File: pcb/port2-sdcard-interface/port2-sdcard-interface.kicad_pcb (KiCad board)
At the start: 4 copper layers, 80 x 100 mm, 58 parts, among them J2 P2000T Port 2, J3 SD Card, U1 CY62128ELL-45SXI, U10 74HC32, U11 74HC273, U12 74HC165, U13 74HC595, U14 74HC00, U15 SST39SF010, U17 74HC138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

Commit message: Adding secondary LEDs
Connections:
- U4 pad 12: ~{S5} -> Net-(U4-Pad12)
- U4 pad 13: ~{S5} -> Net-(U4-Pad12)
- U9 pad 4: ~{S2} -> ~{S5}
- U9 pad 5: ~{RD} -> ~{WR}
- U9 pad 6: unconnected-(U9-Pad6) -> Net-(U4-Pad12)
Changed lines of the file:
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@@
   (net 81 "~{CLKSTART}")
   (net 82 "~{SER_RD}")
-  (net 83 "unconnected-(U9-Pad6)")
+  (net 83 "Net-(U4-Pad12)")
   (net 84 "~{SDOUT_SET}")
   (net 85 "~{SDOUT_RESET}")
@@
       (net 115 "LED_SEL") (pintype "output"))
     (pad "12" smd roundrect (at 2.475 1.27 270) (size 1.95 0.6) (layers "B.Cu" "B.Paste" "B.Mask") (roundrect_rratio 0.25)
-      (net 116 "~{S5}") (pintype "input"))
+      (net 83 "Net-(U4-Pad12)") (pintype "input"))
     (pad "13" smd roundrect (at 2.475 2.54 270) (size 1.95 0.6) (layers "B.Cu" "B.Paste" "B.Mask") (roundrect_rratio 0.25)
-      (net 116 "~{S5}") (pintype "input"))
+      (net 83 "Net-(U4-Pad12)") (pintype "input"))
     (pad "14" smd roundrect (at 2.475 3.81 270) (size 1.95 0.6) (layers "B.Cu" "B.Paste" "B.Mask") (roundrect_rratio 0.25)
       (net 1 "VCC") (pinfunction "VCC") (pintype "power_in"))
@@
       (net 82 "~{SER_RD}") (pintype "output"))
     (pad "4" smd roundrect (at -2.475 0 270) (size 1.95 0.6) (layers "B.Cu" "B.Paste" "B.Mask") (roundrect_rratio 0.25)
-      (net 79 "~{S2}") (pintype "input"))
+      (net 116 "~{S5}") (pintype "input"))
     (pad "5" smd roundrect (at -2.475 -1.27 270) (size 1.95 0.6) (layers "B.Cu" "B.Paste" "B.Mask") (roundrect_rratio 0.25)
-      (net 31 "~{RD}") (pintype "input"))
+      (net 32 "~{WR}") (pintype "input"))
     (pad "6" smd roundrect (at -2.475 -2.54 270) (size 1.95 0.6) (layers "B.Cu" "B.Paste" "B.Mask") (roundrect_rratio 0.25)
-      (net 83 "unconnected-(U9-Pad6)") (pintype "output+no_connect"))
+      (net 83 "Net-(U4-Pad12)") (pintype "output"))
     (pad "7" smd roundrect (at -2.475 -3.81 270) (size 1.95 0.6) (layers "B.Cu" "B.Paste" "B.Mask") (roundrect_rratio 0.25)
       (net 12 "GND") (pinfunction "GND") (pintype "power_in"))
@@
     (connect_pads (clearance 0))
     (min_thickness 0.25) (filled_areas_thickness no)
-    (fill yes (thermal_gap 0.5) (thermal_bridge_width 0.5))
+    (fill (thermal_gap 0.5) (thermal_bridge_width 0.5))
     (polygon
       (pts
@@
     (connect_pads (clearance 0))
     (min_thickness 0.25) (filled_areas_thickness no)
-    (fill yes (thermal_gap 0.5) (thermal_bridge_width 0.5))
+    (fill (thermal_gap 0.5) (thermal_bridge_width 0.5))
     (polygon
       (pts

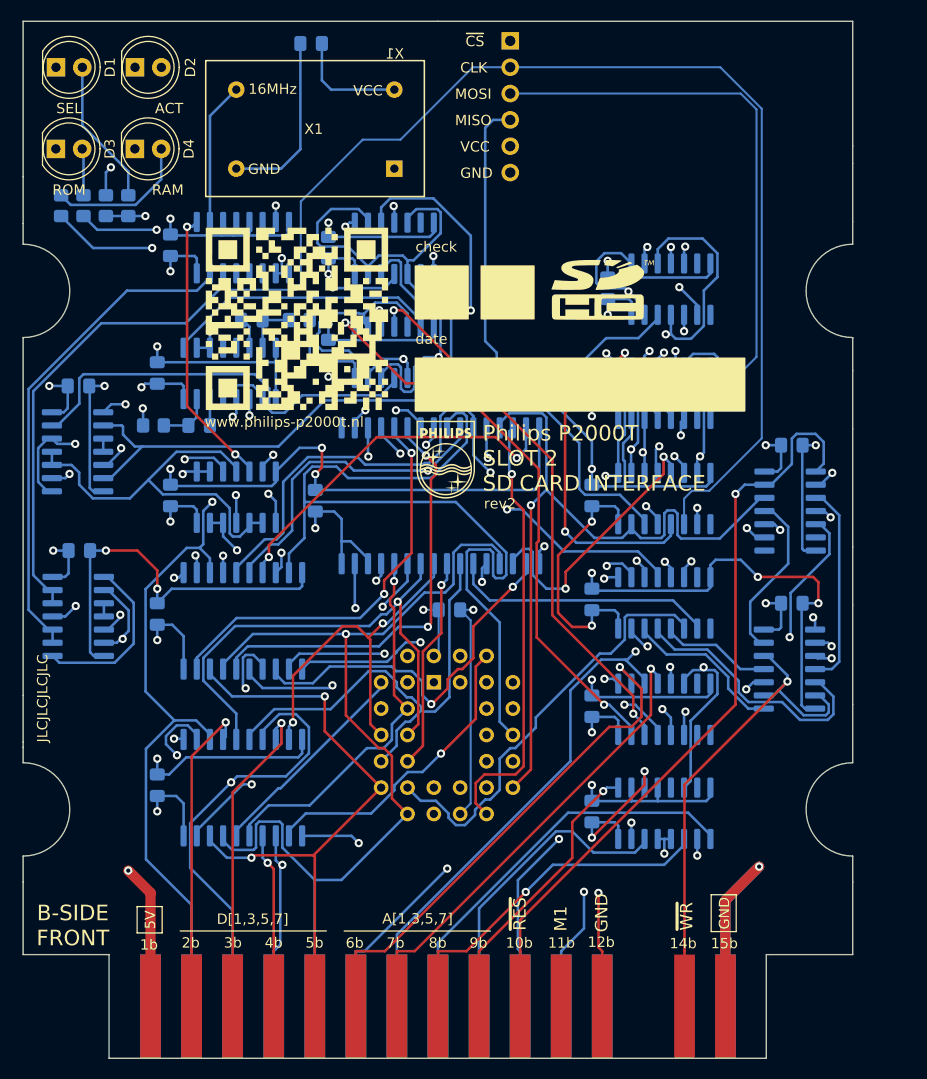
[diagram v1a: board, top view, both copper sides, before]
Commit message: Fixing bug in erroneously triggered LEDs
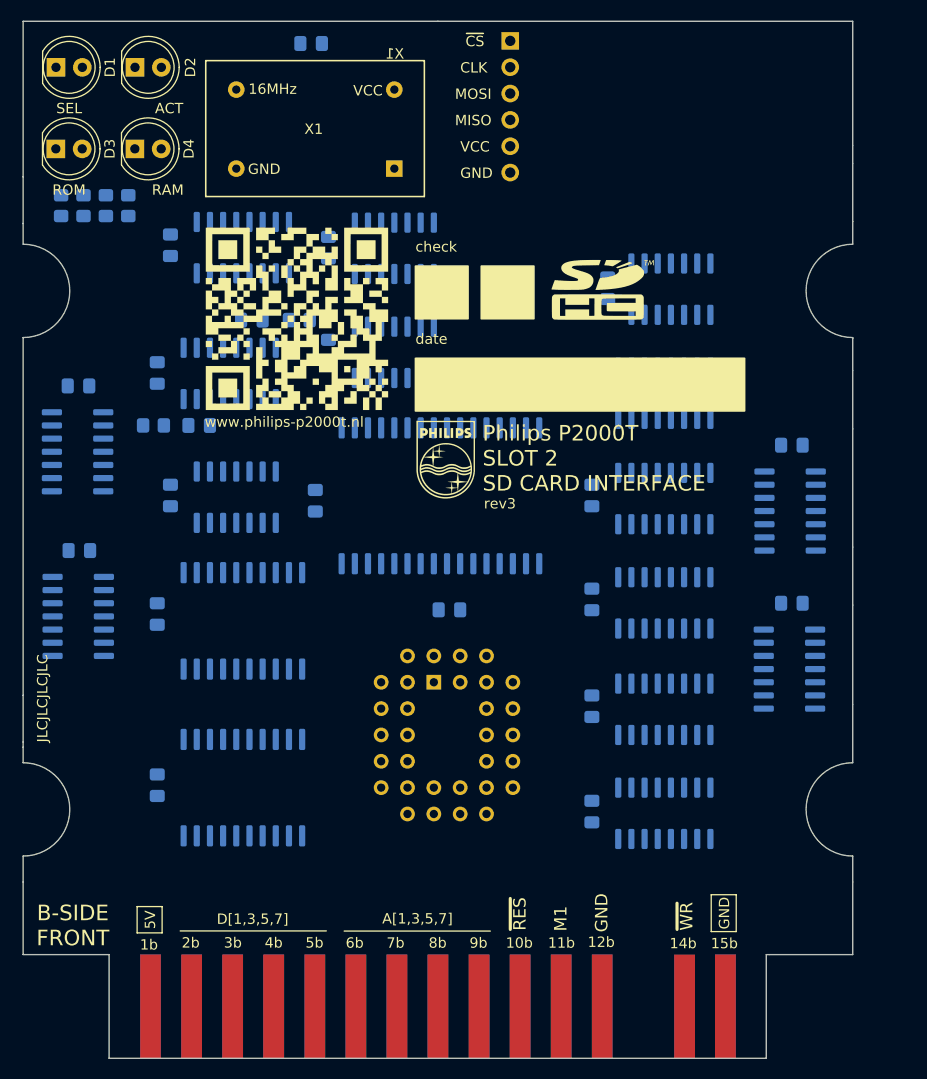
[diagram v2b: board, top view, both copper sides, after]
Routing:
- net GND: track 412.5 -> 0.00 mm, vias 26 -> 0
- net D0: track 230.2 -> 0.00 mm, vias 5 -> 0
- net VCC: track 197.2 -> 0.00 mm, vias 34 -> 0
- net ~{RES}: track 189.6 -> 0.00 mm, vias 4 -> 0
- net D1: track 158.9 -> 0.00 mm, vias 4 -> 0
- net ~{WR}: track 157.8 -> 0.00 mm, vias 4 -> 0
- net CLK: track 156.7 -> 0.00 mm
- net D2: track 152.9 -> 0.00 mm, vias 4 -> 0
- net D6: track 149.6 -> 0.00 mm, vias 3 -> 0
- net A3: track 143.2 -> 0.00 mm, vias 2 -> 0
- net D5: track 132.5 -> 0.00 mm, vias 5 -> 0
- net D7: track 127.4 -> 0.00 mm, vias 4 -> 0
- net D4: track 119.6 -> 0.00 mm, vias 5 -> 0
- net ~{RD}: track 118.8 -> 0.00 mm, vias 3 -> 0
- net D3: track 116.2 -> 0.00 mm, vias 4 -> 0
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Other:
- board text added: "rev3"
- board text removed: "rev2"

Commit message: Fixing bug in RAM/ROM leds
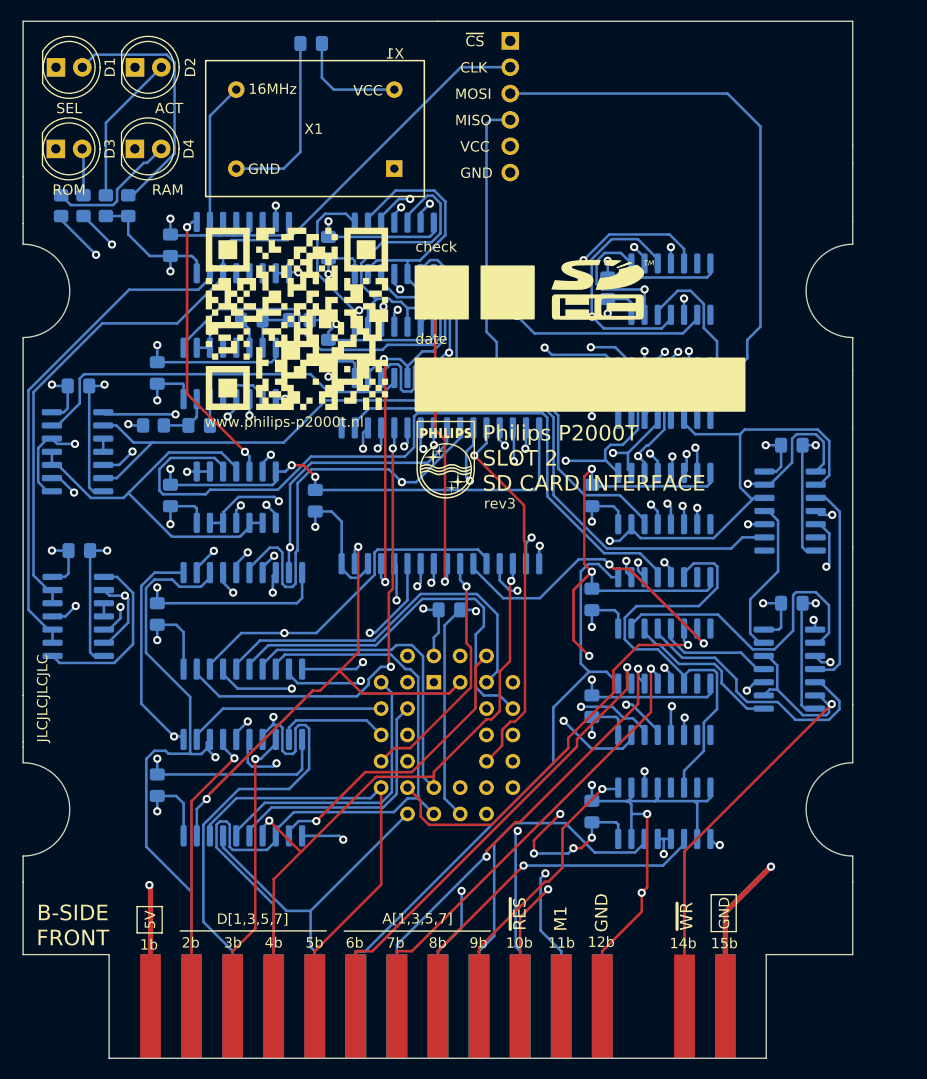
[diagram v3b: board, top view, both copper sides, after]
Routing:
- net GND: track 0.00 -> 419.8 mm, vias 0 -> 25
- net D0: track 0.00 -> 205.1 mm, vias 0 -> 4
- net VCC: track 0.00 -> 193.7 mm, vias 0 -> 37
- net ~{WR}: track 0.00 -> 176.8 mm, vias 0 -> 4
- net ~{RES}: track 0.00 -> 174.0 mm, vias 0 -> 4
- net D7: track 0.00 -> 156.4 mm, vias 0 -> 3
- net D1: track 0.00 -> 151.3 mm, vias 0 -> 4
- net D2: track 0.00 -> 138.7 mm, vias 0 -> 4
- net D4: track 0.00 -> 138.7 mm, vias 0 -> 3
- net A3: track 0.00 -> 134.3 mm, vias 0 -> 2
- net CLK: track 0.00 -> 133.2 mm, vias 0 -> 1
- net D5: track 0.00 -> 127.6 mm, vias 0 -> 4
- net D6: track 0.00 -> 125.8 mm, vias 0 -> 4
- net D3: track 0.00 -> 120.4 mm, vias 0 -> 4
- net ~{RD}: track 0.00 -> 107.2 mm, vias 0 -> 3
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
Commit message: Revising PCB
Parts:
- D3: value ROM -> READ
- D4: value RAM -> WRITE
- R1, R6, R7: value 510 -> 560
- R2: value 510 -> 0
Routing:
- net Net-(U3A-Q): track 62.7 -> 71.9 mm
- net Net-(U3B-Q): track 67.5 -> 73.1 mm
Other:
- board text added: "act"
- board text added: "https://github.com/ifilot/p2000t-sdcard"
- board text added: "read"
- board text added: "rev4"
- board text added: "sel"
- board text added: "write"
- board text removed: "rev3"
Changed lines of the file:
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@@
         (effects (font (size 1 1) (thickness 0.15)))
     )
-    (fp_text value "RAM" (at 3.175 3.96) (layer "F.SilkS")
+    (fp_text value "WRITE" (at 3.175 3.96) (layer "F.SilkS")
         (effects (font (size 1 1) (thickness 0.15)))
     )
@@
         (effects (font (size 1 1) (thickness 0.15)))
     )
-    (fp_text value "ROM" (at 1.27 3.96) (layer "F.SilkS")
+    (fp_text value "READ" (at 1.27 3.96) (layer "F.SilkS")
         (effects (font (size 1 1) (thickness 0.15)))
     )
@@
         (effects (font (size 1 1) (thickness 0.15)) (justify mirror))
     )
-    (fp_text value "510" (at 0 -1.65 90) (layer "B.Fab")
-        (effects (font (size 1 1) (thickness 0.15)) (justify mirror))
+    (fp_text value "560" (at -4.556 0.127 90) (layer "B.SilkS")
+        (effects (font (size 0.7 0.7) (thickness 0.1)) (justify mirror))
     )
     (fp_text user "${REFERENCE}" (at 0 0 90) (layer "B.Fab")
@@
         (effects (font (size 1 1) (thickness 0.15)) (justify mirror))
     )
-    (fp_text value "510" (at 0 -1.65 90) (layer "B.Fab")
-        (effects (font (size 1 1) (thickness 0.15)) (justify mirror))
+    (fp_text value "560" (at -4.556 0.381 270) (layer "B.SilkS")
+        (effects (font (size 0.7 0.7) (thickness 0.1) bold) (justify mirror))
     )
     (fp_text user "${REFERENCE}" (at 0 0 90) (layer "B.Fab")
@@
         (effects (font (size 1 1) (thickness 0.15)) (justify mirror))
     )
-    (fp_text value "510" (at 0 -1.65 90) (layer "B.Fab")
-        (effects (font (size 1 1) (thickness 0.15)) (justify mirror))
+    (fp_text value "560" (at 4.556 0.254 90) (layer "B.SilkS")
+        (effects (font (size 0.7 0.7) (thickness 0.1)) (justify mirror))
     )
     (fp_text user "${REFERENCE}" (at 0 0 90) (layer "B.Fab")
@@
         (effects (font (size 1 1) (thickness 0.15)) (justify mirror))
     )
-    (fp_text value "510" (at 0 -1.65 90) (layer "B.Fab")
-        (effects (font (size 1 1) (thickness 0.15)) (justify mirror))
+    (fp_text value "0" (at 3.794 0.254 90) (layer "B.SilkS")
+        (effects (font (size 0.7 0.7) (thickness 0.1)) (justify mirror))
     )
     (fp_text user "${REFERENCE}" (at 0 0 90) (layer "B.Fab")
@@
     (effects (font (size 1 1) (thickness 0.15)) (justify mirror))
   )
+  (gr_text "act" (at 29.953 31.736 90) (layer "B.SilkS")
+    (effects (font (size 0.7 0.7) (thickness 0.1)) (justify left bottom mirror))
+  )
   (gr_text "MISO" (at 64.751 27.926) (layer "B.SilkS")
     (effects (font (size 1 1) (thickness 0.15)) (justify left bottom mirror))
@@
     (effects (font (size 1 1) (thickness 0.15)) (justify left bottom mirror))
   )
+  (gr_text "sel" (at 32.112 31.99 90) (layer "B.SilkS")
+    (effects (font (size 0.7 0.7) (thickness 0.1)) (justify left bottom mirror))
+  )
+  (gr_text "read" (at 27.794 31.228 90) (layer "B.SilkS")
+    (effects (font (size 0.7 0.7) (thickness 0.1)) (justify left bottom mirror))
+  )
   (gr_text "2a" (at 37.7497 106.6421) (layer "B.SilkS")
     (effects (font (size 1 1) (thickness 0.15)) (justify mirror))
@@
     (effects (font (size 1.2 1.2) (thickness 0.3)) (justify mirror))
   )
+  (gr_text "write" (at 25.508 31.228 90) (layer "B.SilkS")
+    (effects (font (size 0.7 0.7) (thickness 0.1)) (justify left bottom mirror))
+  )
   (gr_text "MISO" (at 73.26 53.199) (layer "B.SilkS")
     (effects (font (size 1 1) (thickness 0.15)) (justify left bottom mirror))
@@
     (effects (font (size 1 1) (thickness 0.15)) (justify left bottom))
   )
-  (gr_text "rev3" (at 66.021 64.883) (layer "F.SilkS")
+  (gr_text "rev4" (at 66.021 64.883) (layer "F.SilkS")
     (effects (font (size 1 1) (thickness 0.15)) (justify left bottom))
   )
@@
     (effects (font (size 1 1) (thickness 0.15)))
   )
+  (gr_text "https://github.com/ifilot/p2000t-sdcard" (at 59.417 66.915) (layer "F.SilkS")
+    (effects (font (size 1 1) (thickness 0.15)) (justify left bottom))
+  )
   (gr_text "date" (at 59.417 49.008) (layer "F.SilkS")
     (effects (font (size 1 1) (thickness 0.15)) (justify left bottom))
@@
   (segment (start 94.3897 70.8312) (end 94.3897 65.9414) (width 0.25) (layer "B.Cu") (net 109))
   (segment (start 91.7087 73.5122) (end 94.3897 70.8312) (width 0.25) (layer "B.Cu") (net 109))
-  (via (at 30.16 39.3067) (size 0.8) (drill 0.4) (layers "F.Cu" "B.Cu") (net 113))
+  (via (at 29.445 44.436) (size 0.8) (drill 0.4) (layers "F.Cu" "B.Cu") (net 113))
   (via (at 75.6266 40.8266) (size 0.8) (drill 0.4) (layers "F.Cu" "B.Cu") (net 113))
-  (segment (start 75.6266 40.8266) (end 74.1067 39.3067) (width 0.25) (layer "In1.Cu") (net 113))
-  (segment (start 74.1067 39.3067) (end 30.16 39.3067) (width 0.25) (layer "In1.Cu") (net 113))
+  (segment (start 31.731 39.61) (end 29.445 41.896) (width 0.25) (layer "In1.Cu") (net 113))
+  (segment (start 75.6266 40.8266) (end 74.1525 39.3525) (width 0.25) (layer "In1.Cu") (net 113))
+  (segment (start 29.445 41.896) (end 29.445 44.436) (width 0.25) (layer "In1.Cu") (net 113))
+  (segment (start 74.1525 39.3525) (end 31.9885 39.3525) (width 0.25) (layer "In1.Cu") (net 113))
+  (segment (start 74.1525 39.3525) (end 74.1067 39.3067) (width 0.25) (layer "In1.Cu") (net 113))
+  (segment (start 31.9885 39.3525) (end 31.731 39.61) (width 0.25) (layer "In1.Cu") (net 113))
   (segment (start 85.325 41.137) (end 85.325 39.7371) (width 0.25) (layer "B.Cu") (net 113))
   (segment (start 78.1117 38.3415) (end 75.6266 40.8266) (width 0.25) (layer "B.Cu") (net 113))
+  (segment (start 27.413 36.562) (end 27.413 40.626) (width 0.25) (layer "B.Cu") (net 113))
   (segment (start 27.4153 36.562) (end 27.413 36.562) (width 0.25) (layer "B.Cu") (net 113))
-  (segment (start 30.16 39.3067) (end 27.4153 36.562) (width 0.25) (layer "B.Cu") (net 113))
+  (segment (start 27.413 40.626) (end 29.445 42.658) (width 0.25) (layer "B.Cu") (net 113))
+  (segment (start 29.445 42.658) (end 29.445 44.436) (width 0.25) (layer "B.Cu") (net 113))
   (segment (start 83.9294 38.3415) (end 78.1117 38.3415) (width 0.25) (layer "B.Cu") (net 113))
   (segment (start 85.325 39.7371) (end 83.9294 38.3415) (width 0.25) (layer "B.Cu") (net 113))
-  (via (at 28.6251 40.2989) (size 0.8) (drill 0.4) (layers "F.Cu" "B.Cu") (net 114))
   (via (at 69.2158 46.1938) (size 0.8) (drill 0.4) (layers "F.Cu" "B.Cu") (net 114))
+  (via (at 27.667 44.436) (size 0.8) (drill 0.4) (layers "F.Cu" "B.Cu") (net 114))
   (segment (start 69.2158 46.1938) (end 65.6207 42.5987) (width 0.25) (layer "In1.Cu") (net 114))
+  (segment (start 30.207 45.198) (end 28.429 45.198) (width 0.25) (layer "In1.Cu") (net 114))
+  (segment (start 31.2305 42.9043) (end 31.2305 44.1745) (width 0.25) (layer "In1.Cu") (net 114))
   (segment (start 62.0797 42.5987) (end 61.7741 42.9043) (width 0.25) (layer "In1.Cu") (net 114))
   (segment (start 65.6207 42.5987) (end 62.0797 42.5987) (width 0.25) (layer "In1.Cu") (net 114))
-  (segment (start 31.2305 42.9043) (end 28.6251 40.2989) (width 0.25) (layer "In1.Cu") (net 114))
+  (segment (start 28.429 45.198) (end 27.667 44.436) (width 0.25) (layer "In1.Cu") (net 114))
+  (segment (start 31.2305 44.1745) (end 30.207 45.198) (width 0.25) (layer "In1.Cu") (net 114))
   (segment (start 61.7741 42.9043) (end 31.2305 42.9043) (width 0.25) (layer "In1.Cu") (net 114))
-  (segment (start 28.6251 40.2989) (end 25.254 36.9278) (width 0.25) (layer "B.Cu") (net 114))
+  (segment (start 25.254 36.562) (end 25.254 39.737) (width 0.25) (layer "B.Cu") (net 114))
+  (segment (start 27.667 42.15) (end 27.667 44.436) (width 0.25) (layer "B.Cu") (net 114))
   (segment (start 85.2064 47.8818) (end 70.9038 47.8818) (width 0.25) (layer "B.Cu") (net 114))
-  (segment (start 25.254 36.9278) (end 25.254 36.562) (width 0.25) (layer "B.Cu") (net 114))
   (segment (start 86.595 46.087) (end 86.595 46.4932) (width 0.25) (layer "B.Cu") (net 114))
   (segment (start 86.595 46.4932) (end 85.2064 47.8818) (width 0.25) (layer "B.Cu") (net 114))
   (segment (start 70.9038 47.8818) (end 69.2158 46.1938) (width 0.25) (layer "B.Cu") (net 114))
+  (segment (start 25.254 39.737) (end 27.667 42.15) (width 0.25) (layer "B.Cu") (net 114))
   (via (at 42.5866 64.4691) (size 0.8) (drill 0.4) (layers "F.Cu" "B.Cu") (net 115))
   (via (at 76.4507 46.2616) (size 0.8) (drill 0.4) (layers "F.Cu" "B.Cu") (net 115))

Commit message: Changing PCB to also accept SST39SF020 and SST39SF040 chips
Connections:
- U15 pad 1: unconnected-(U15-NC-Pad1) -> GND
- U15 pad 30: unconnected-(U15-NC-Pad30) -> GND
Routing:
- net GND: track 419.8 -> 448.9 mm, vias 25 -> 27
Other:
- board text added: "rev5"
- board text removed: "rev4"

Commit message: Changing resistor value
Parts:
- R6: value 560 -> 180
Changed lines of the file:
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@@
         (effects (font (size 1 1) (thickness 0.15)) (justify mirror))
     )
-    (fp_text value "560" (at -4.556 0.127 90) (layer "B.SilkS")
+    (fp_text value "180" (at -4.556 0.127 90) (layer "B.SilkS")
         (effects (font (size 0.7 0.7) (thickness 0.1)) (justify mirror))
     )
